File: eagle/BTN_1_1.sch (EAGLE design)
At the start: 24 parts, among them IC1 74HC14N, X1 Out, X2 Out

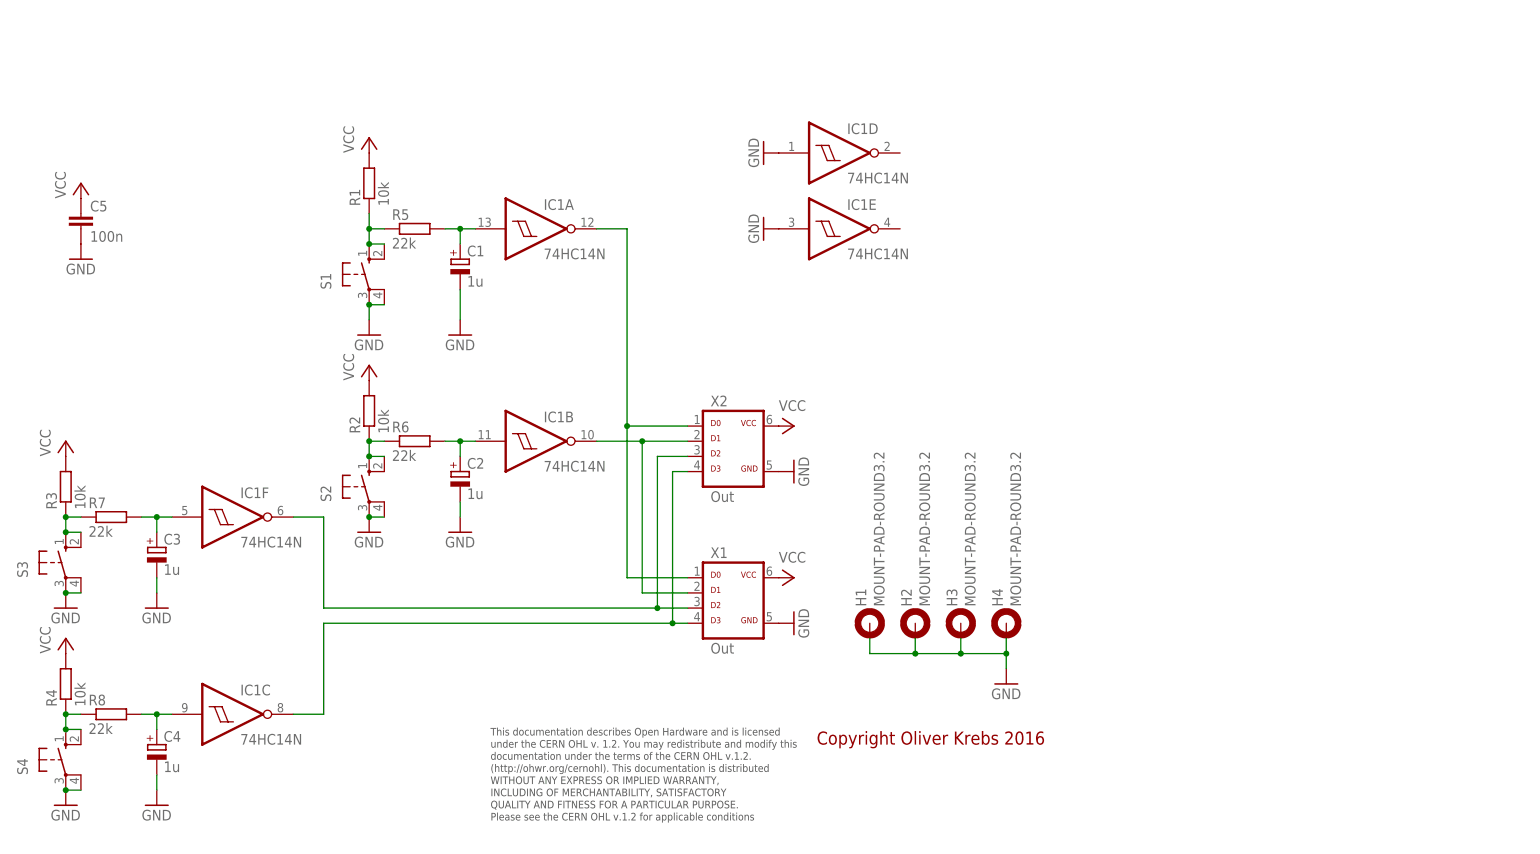
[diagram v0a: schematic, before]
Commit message: Add new tetra-Board and arduino files
Add AMP_1_0, AVC_1_0, D18_1_1, IOP_1_2, MIC_1_0, PIN_1_1, POT_1_0, PWA_1_0, PWR_1_0, RGF 2.0, SOC_2_0, VLT_1_0
Add mex_nano_shield_keyboard, mex_nano_shied_numbers

New arduino projects
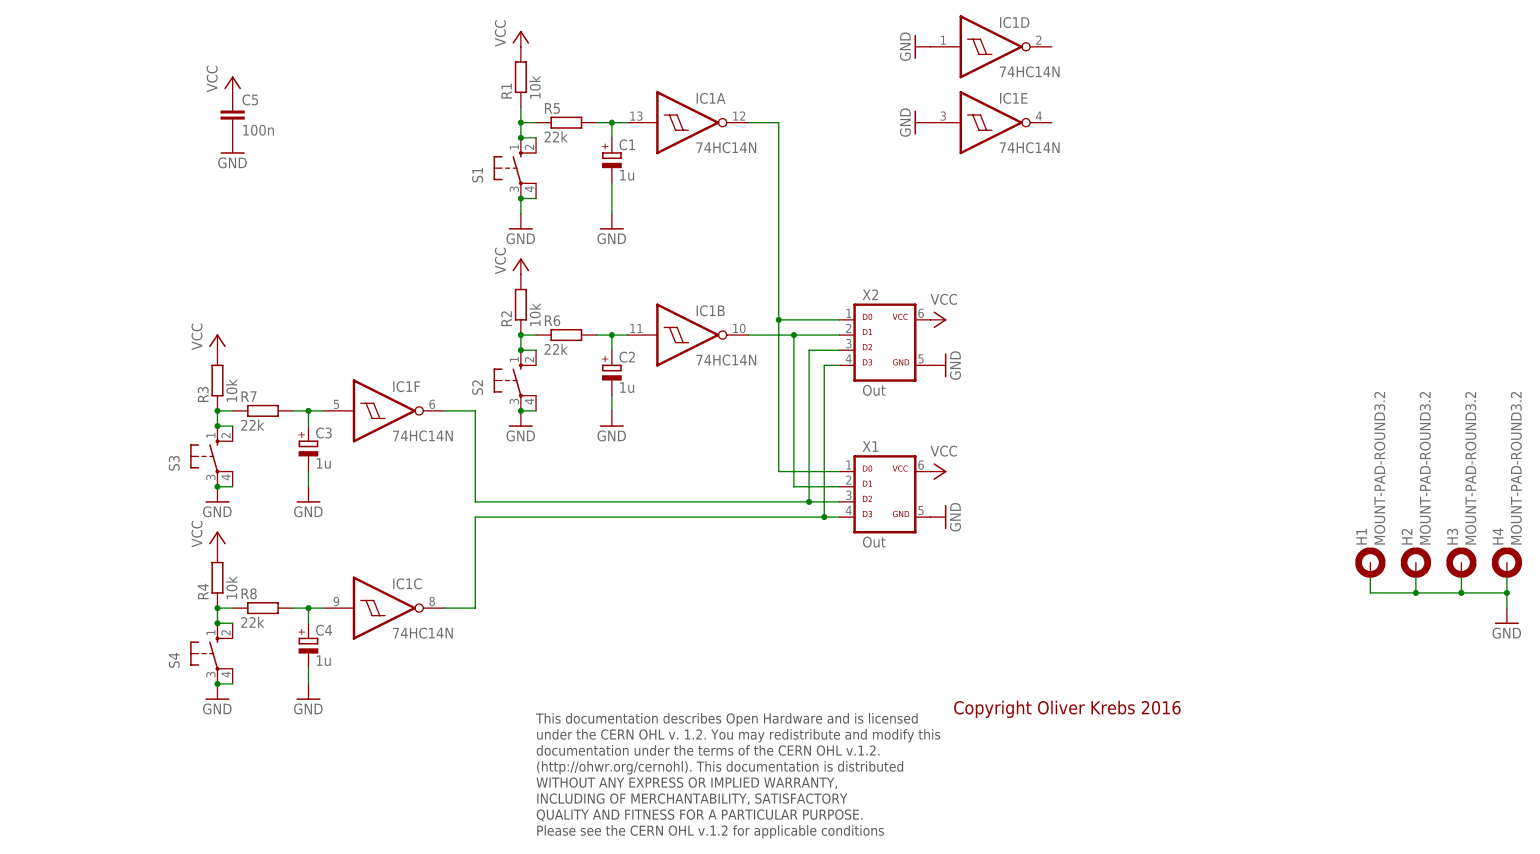
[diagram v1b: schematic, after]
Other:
- moved on the sheet: C1, C2, C3, C4, C5, H1, H2, H3, H4, IC1A, IC1B, IC1C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
